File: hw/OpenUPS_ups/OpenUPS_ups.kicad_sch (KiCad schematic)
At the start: 20 parts, among them J101 XT30PW-M, J102 Barrel Jack, J103 Screw Terminal, J104 Screw Terminal, J105 Screw Terminal, J106 JST XH, J107 JST XH, J108 XT30PW-M, J109 JST_SH_SM02B, J110 JST_SH_SM02B, U102 AVR32DB48x-xPT

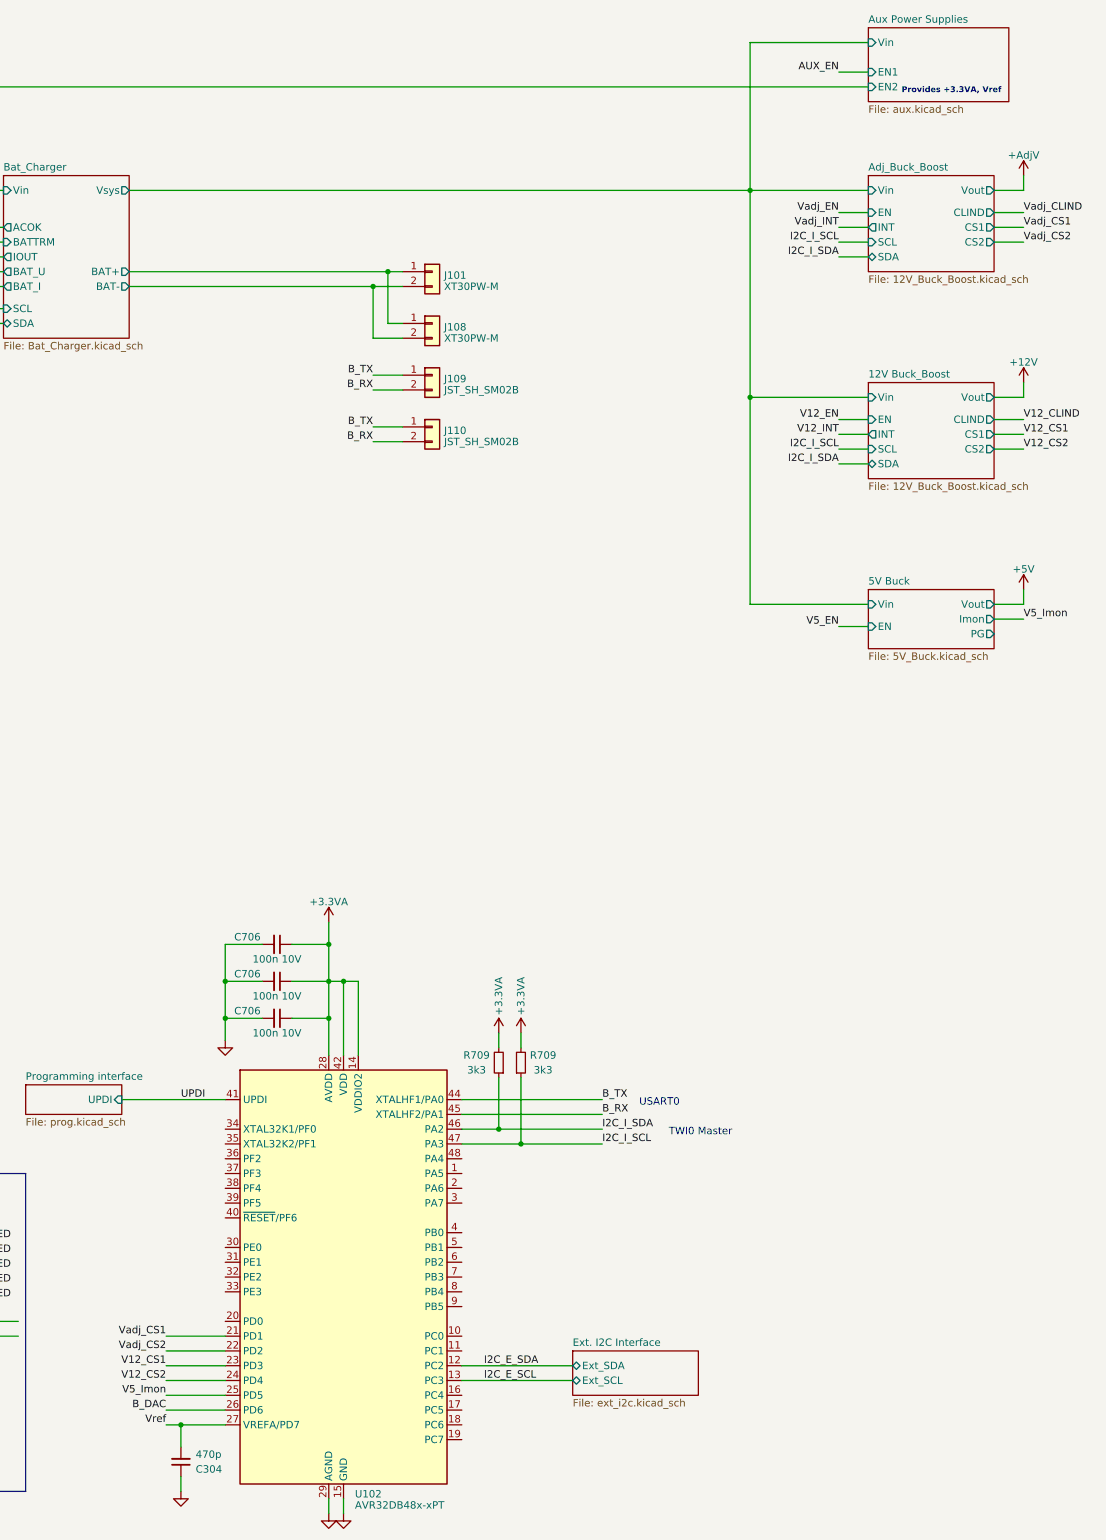
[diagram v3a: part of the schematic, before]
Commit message: Removed Vref (AVR has its own). Replaced INA181s with INA180s
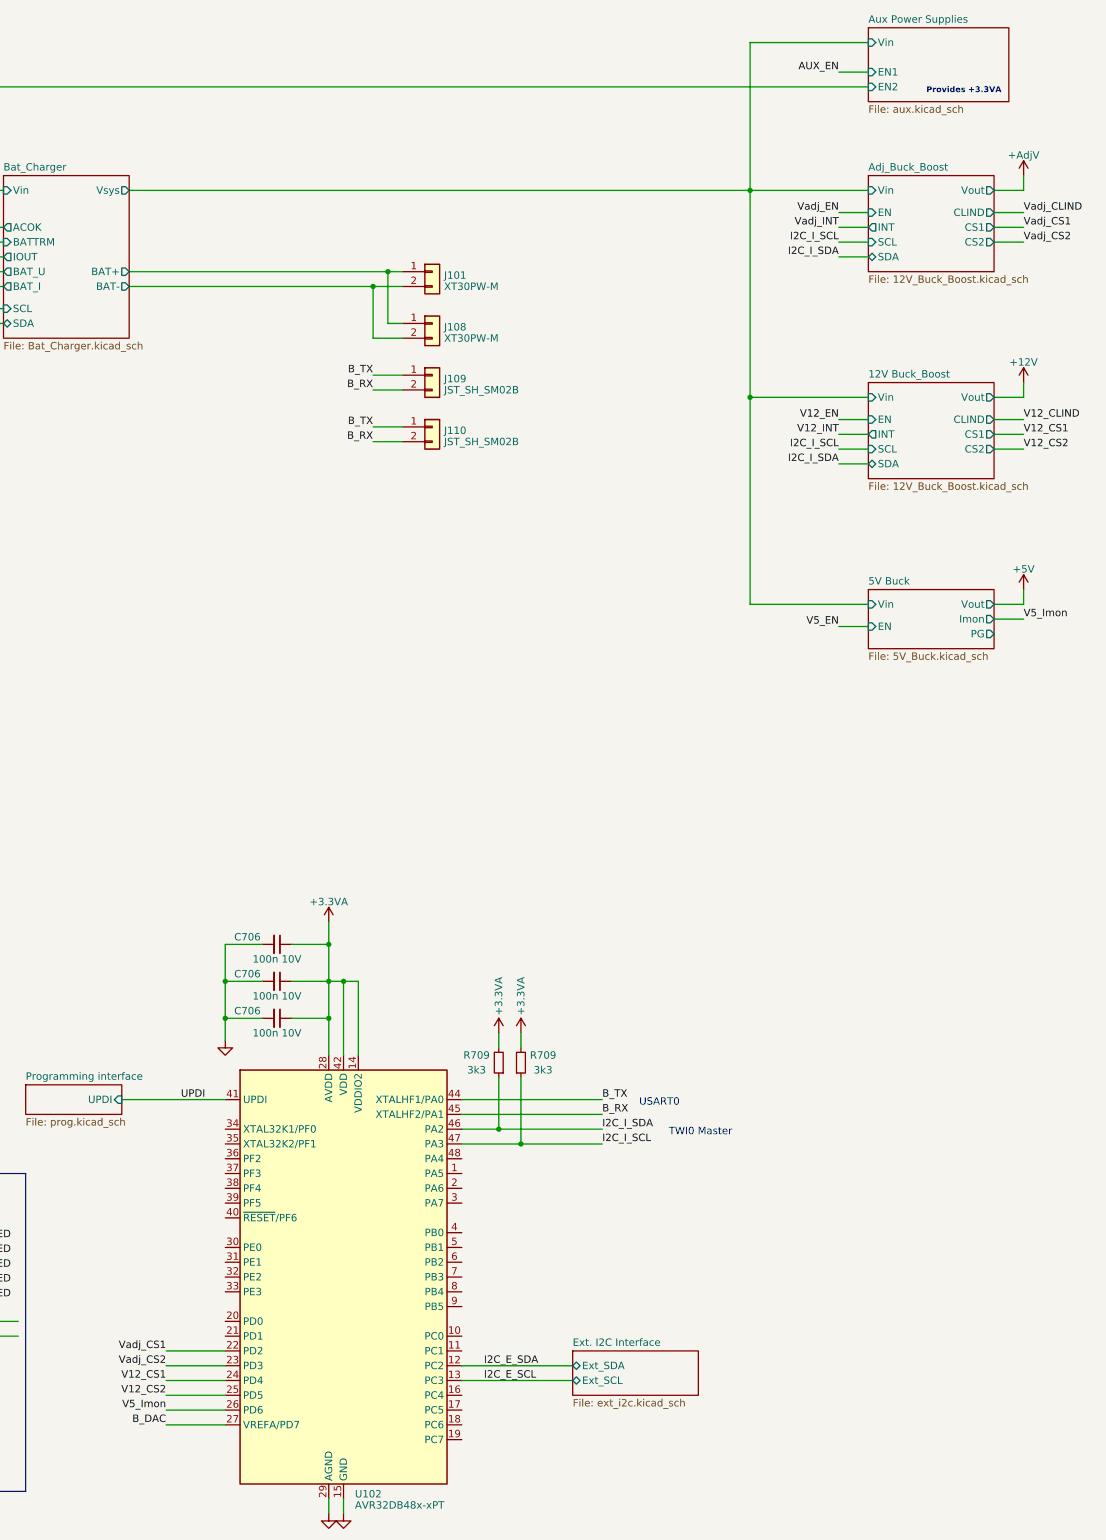
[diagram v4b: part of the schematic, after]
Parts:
- removed C304: 470p, Capacitor_SMD:C_0603_1608Metric, symbol Device:C_Small
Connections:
- net Vref is gone; now on net B_DAC: U102.27 (VREFA/PD7)
- net B_DAC: no longer U102.26 (PD6)
- net V12_CS1: now also U102.24 (PD4); no longer U102.23 (PD3)
- net V12_CS2: now also U102.25 (PD5); no longer U102.24 (PD4)
- net V5_Imon: now also U102.26 (PD6); no longer U102.25 (PD5)
- net Vadj_CS1: now also U102.22 (PD2); no longer U102.21 (PD1)
- net Vadj_CS2: now also U102.23 (PD3); no longer U102.22 (PD2)
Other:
- note added: "Provides +3.3VA"
- note removed: "Provides +3.3VA, Vref"

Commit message: Initial placement effort
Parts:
- added H101, H102, H103, H104: MountingHole, MountingHole:MountingHole_3.2mm_M3_DIN965, symbol Mechanical:MountingHole
- renumbered J102 to J101, J101 to J102, J108 to J103, J109 to J104, J110 to J105, J103 to J106, J104 to J107, J105 to J108, J106 to J109, J107 to J110, U102 to U101

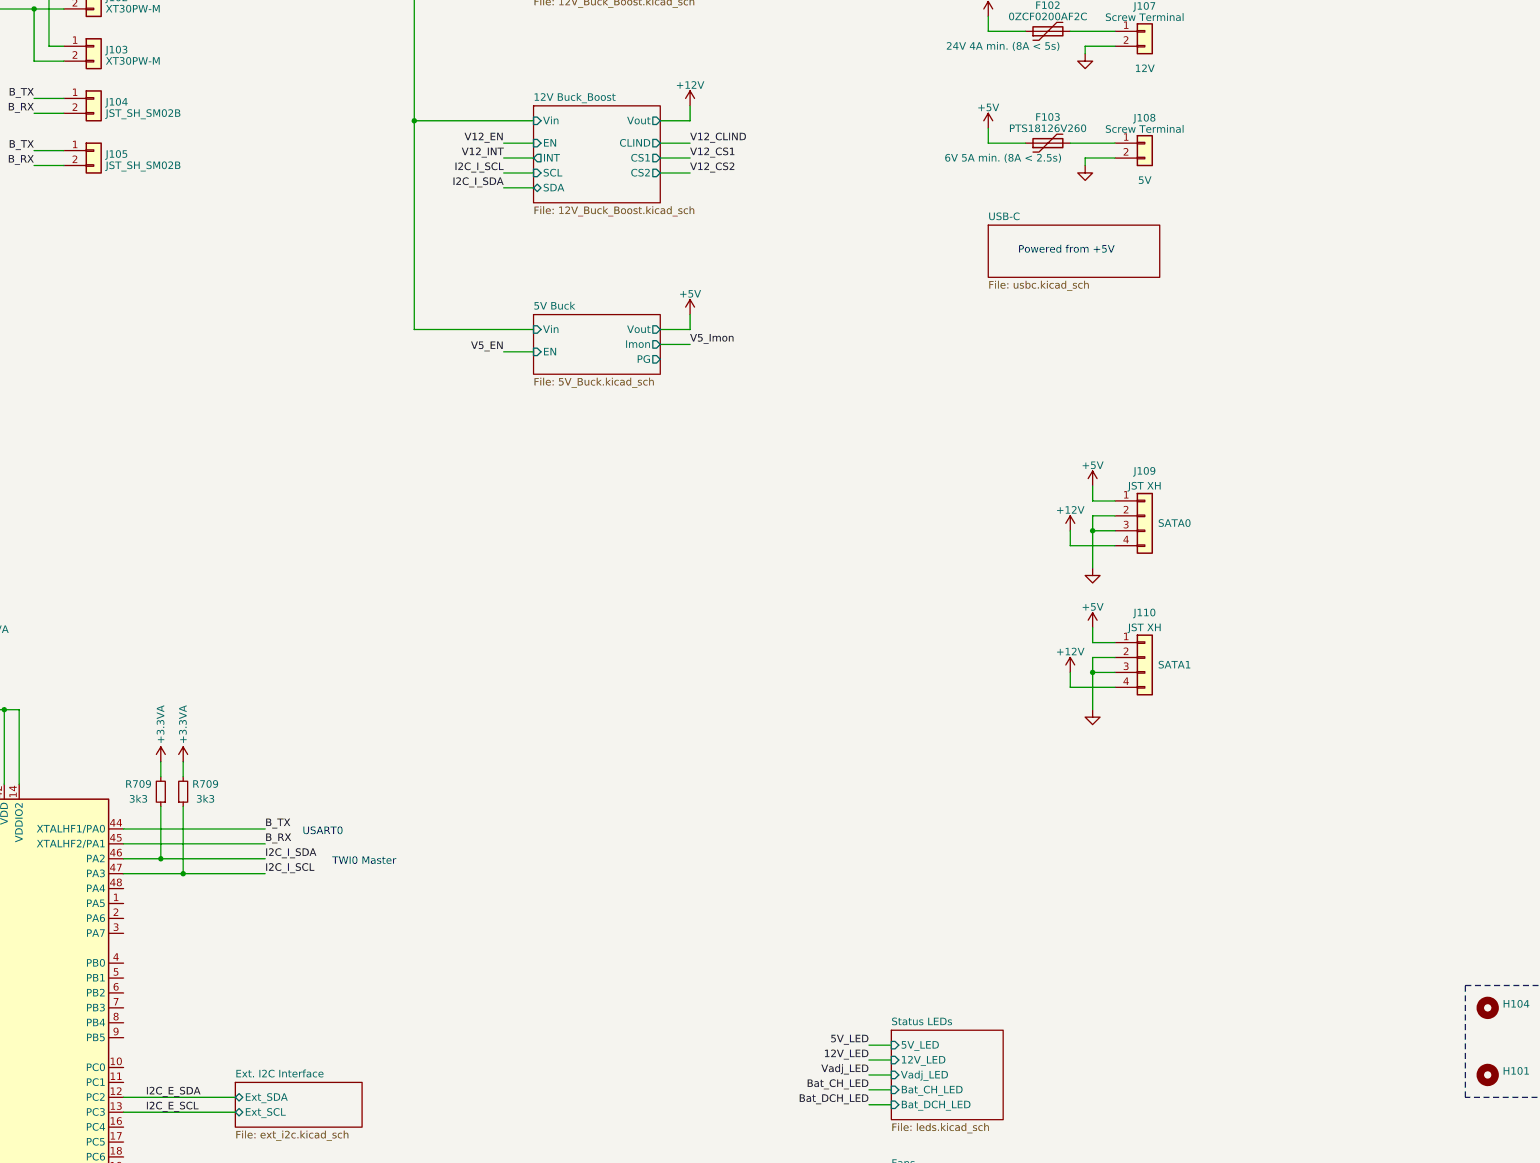
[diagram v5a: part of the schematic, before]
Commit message: Layout: Component models, mechanical, connectors
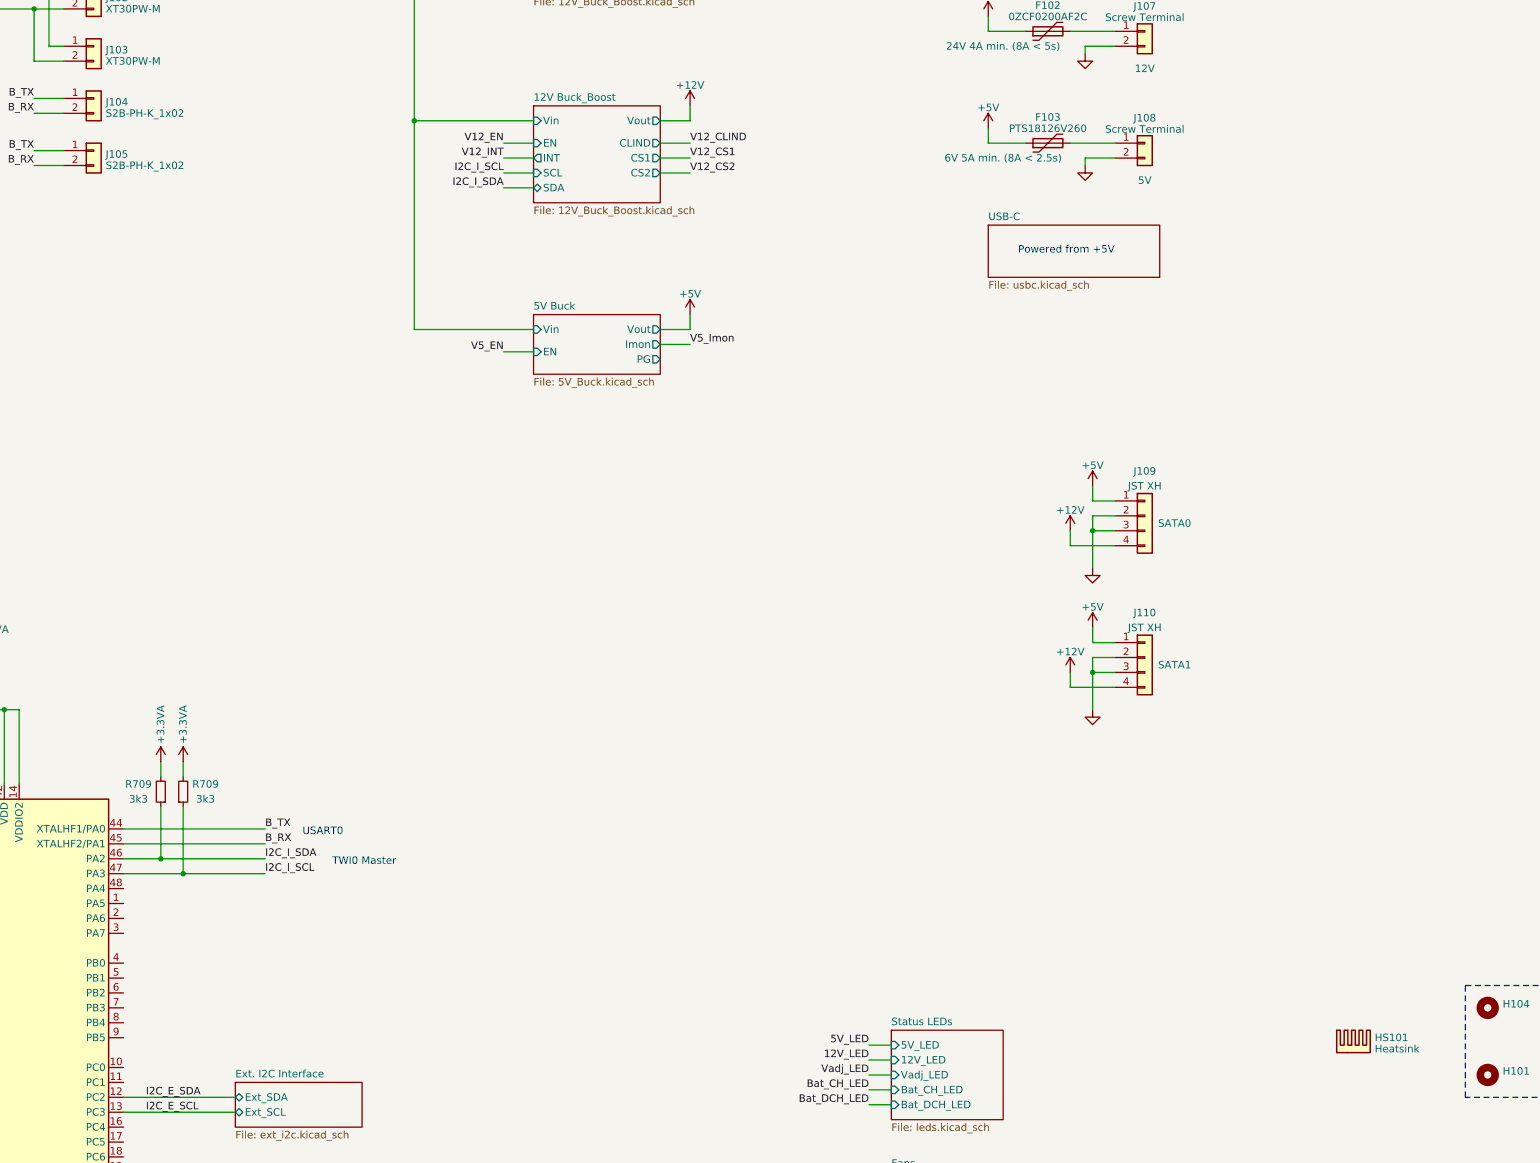
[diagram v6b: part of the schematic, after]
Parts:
- added HS101: Heatsink, OpenUPS_ups:C4_heatsink, symbol Mechanical:Heatsink
- J104, J105: value JST_SH_SM02B -> S2B-PH-K_1x02; footprint Connector_JST:JST_SH_SM02B-SRSS-TB_1x02-1MP_P1.00mm_Horizontal -> Connector_JST:JST_PH_S2B-PH-K_1x02_P2.00mm_Horizontal
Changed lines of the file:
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@@
       (effects (font (size 1.27 1.27)) (justify left))
     )
-    (property "Value" "JST_SH_SM02B" (at 135.382 80.0173 0)
-      (effects (font (size 1.27 1.27)) (justify left))
-    )
-    (property "Footprint" "Connector_JST:JST_SH_SM02B-SRSS-TB_1x02-1MP_P1.00mm_Horizontal" (at 133.35 77.47 0)
+    (property "Value" "S2B-PH-K_1x02" (at 135.382 80.0173 0)
+      (effects (font (size 1.27 1.27)) (justify left))
+    )
+    (property "Footprint" "Connector_JST:JST_PH_S2B-PH-K_1x02_P2.00mm_Horizontal" (at 133.35 77.47 0)
       (effects (font (size 1.27 1.27)) hide)
     )
@@
     )
   )
-  (symbol (lib_id "Connector_Generic:Conn_01x02") (at 133.35 86.36 0) (unit 1)
-    (in_bom yes) (on_board yes) (dnp no) (fields_autoplaced)
-    (property "Reference" "J105" (at 135.382 86.9863 0)
-      (effects (font (size 1.27 1.27)) (justify left))
-    )
-    (property "Value" "JST_SH_SM02B" (at 135.382 88.9073 0)
-      (effects (font (size 1.27 1.27)) (justify left))
-    )
-    (property "Footprint" "Connector_JST:JST_SH_SM02B-SRSS-TB_1x02-1MP_P1.00mm_Horizontal" (at 133.35 86.36 0)
-      (effects (font (size 1.27 1.27)) hide)
-    )
-    (property "Datasheet" "~" (at 133.35 86.36 0)
-      (effects (font (size 1.27 1.27)) hide)
-    )
-    (pin "1")
-    (pin "2")
-    (instances
-      (project "OpenUPS_ups"
-        (path "/f77faec3-eac4-47f3-a2de-ec4a039f4502"
-          (reference "J105") (unit 1)
-        )
-      )
-    )
-  )
   (symbol (lib_id "Device:C_Small") (at 106.68 187.96 270) (mirror x) (unit 1)
     (in_bom yes) (on_board yes) (dnp no)
@@
     )
   )
+  (symbol (lib_id "Connector_Generic:Conn_01x02") (at 133.35 86.36 0) (unit 1)
+    (in_bom yes) (on_board yes) (dnp no) (fields_autoplaced)
+    (property "Reference" "J105" (at 135.382 86.9863 0)
+      (effects (font (size 1.27 1.27)) (justify left))
+    )
+    (property "Value" "S2B-PH-K_1x02" (at 135.382 88.9073 0)
+      (effects (font (size 1.27 1.27)) (justify left))
+    )
+    (property "Footprint" "Connector_JST:JST_PH_S2B-PH-K_1x02_P2.00mm_Horizontal" (at 133.35 86.36 0)
+      (effects (font (size 1.27 1.27)) hide)
+    )
+    (property "Datasheet" "~" (at 133.35 86.36 0)
+      (effects (font (size 1.27 1.27)) hide)
+    )
+    (pin "1")
+    (pin "2")
+    (instances
+      (project "OpenUPS_ups"
+        (path "/f77faec3-eac4-47f3-a2de-ec4a039f4502"
+          (reference "J105") (unit 1)
+        )
+      )
+    )
+  )
   (symbol (lib_id "power:+12V") (at 299.72 151.13 0) (unit 1)
     (in_bom yes) (on_board yes) (dnp no) (fields_autoplaced)
@@
         )
       )
+    )
+  )
+  (symbol (lib_id "Mechanical:Heatsink") (at 347.98 240.03 0) (unit 1)
+    (in_bom yes) (on_board yes) (dnp no) (fields_autoplaced)
+    (property "Reference" "HS101" (at 351.5868 237.4813 0)
+      (effects (font (size 1.27 1.27)) (justify left))
+    )
+    (property "Value" "Heatsink" (at 351.5868 239.4023 0)
+      (effects (font (size 1.27 1.27)) (justify left))
+    )
+    (property "Footprint" "OpenUPS_ups:C4_heatsink" (at 348.2848 240.03 0)
+      (effects (font (size 1.27 1.27)) hide)
+    )
+    (property "Datasheet" "~" (at 348.2848 240.03 0)
+      (effects (font (size 1.27 1.27)) hide)
+    )
+    (instances
+      (project "OpenUPS_ups"
+        (path "/f77faec3-eac4-47f3-a2de-ec4a039f4502"
+          (reference "HS101") (unit 1)
+        )
+      )
